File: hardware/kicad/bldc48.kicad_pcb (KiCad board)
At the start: 4 copper layers, 188 x 74 mm, 174 parts, among them J1 BAT+, J10 BRAKE, J11 POWER_BTN, J12 UART, J2 BAT-, J3 MOTOR_A, J4 MOTOR_B, J5 MOTOR_C, J6 SWD, J7 HALL, J8 THROTTLE, J9 FWD/REV, Q1 MMBTA92, Q2 MMBTA42, Q3 IPT015N10N5, Q4 IPT015N10N5, Q5 IPT015N10N5, Q6 IPT015N10N5, Q7 IPT015N10N5, Q8 IPT015N10N5, U1 LM5164DDA, U10 STM32G431CBT6, U2 LM5164DDA, U3 AP2112K-3.3, U4 LM5109BMA, U5 INA240A1D, U6 LM5109BMA, U7 INA240A1D, U8 LM5109BMA, U9 INA240A1D

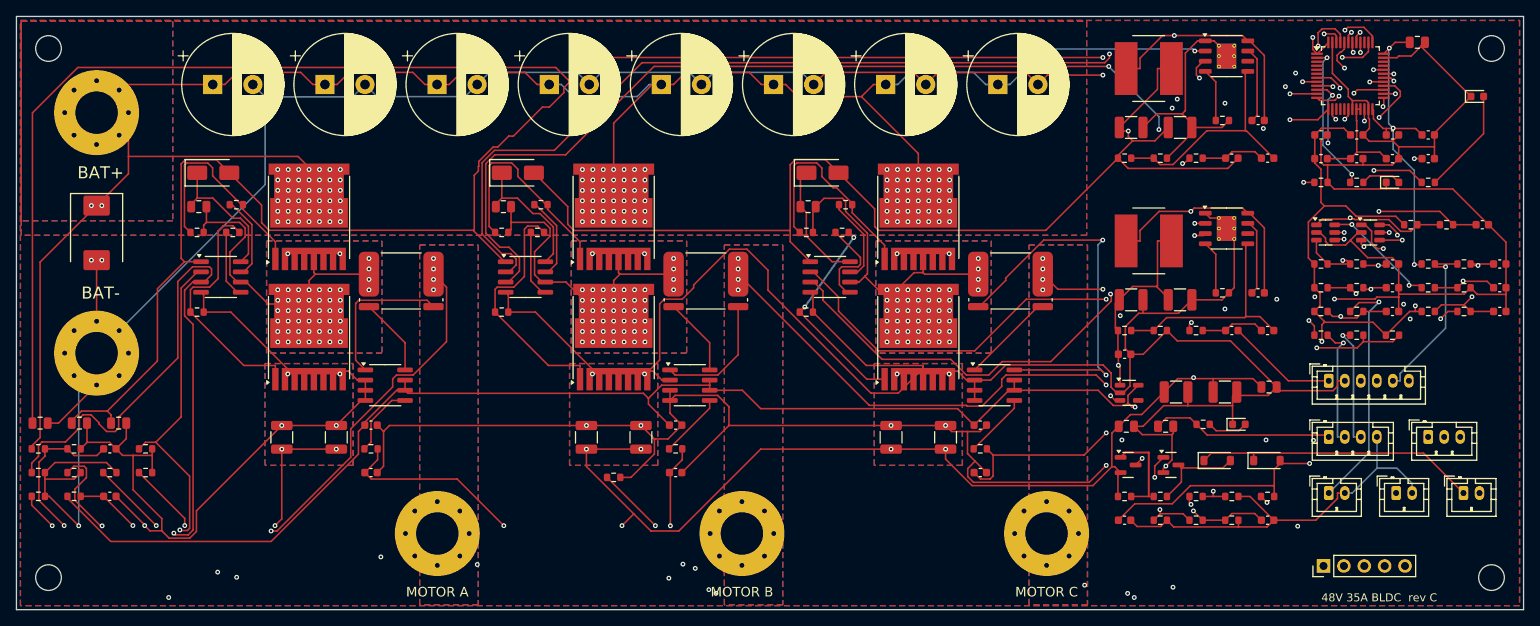
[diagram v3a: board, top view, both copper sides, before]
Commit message: Rev D: 185 x 66 mm board, routed, DRC clean, all parts stocked at LCSC
- Motor terminals beside the DC-link ceramics, routing channel underneath;
  17 mm battery strip; skyline-packed controller strip
- Phase strips free of signal tracks (both layers carry the motor current)
- Two INA240 supply taps the router left open closed with recorded routes
- Aishi ERS1KM221W25OT bulk caps (LCSC C106684)
- New renders, layer images, BOM, schematic PDF; README rev D + cost

Co-Authored-By: Claude Opus 5.5 <noreply@anthropic.com>
Claude-Session: https://claude.ai/code/session_01KE5bAkgcicsoh5erUtagKE
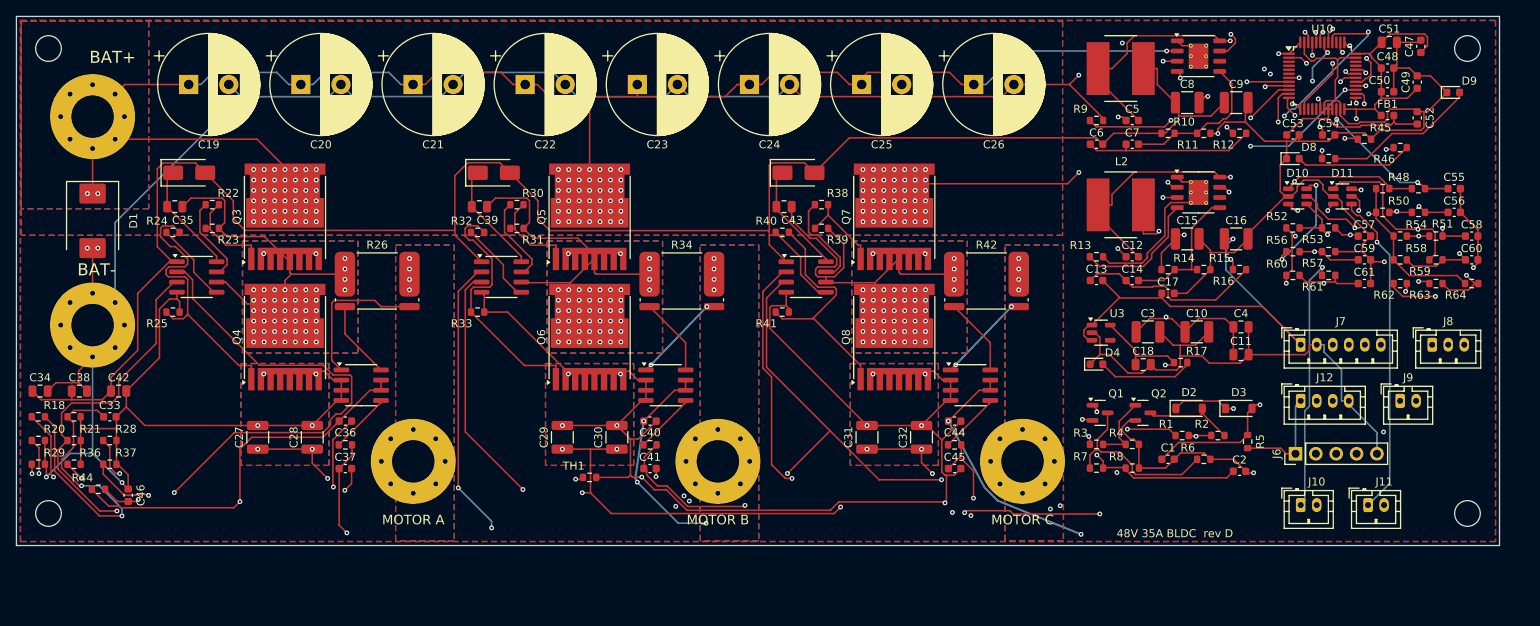
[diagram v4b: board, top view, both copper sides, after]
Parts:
- moved D4 19.3 mm to (134.7, 43.4)
- moved C13 18.0 mm to (134.7, 32.9)
- moved C14 18.0 mm to (139.2, 32.9)
- moved R52 17.5 mm to (159.2, 26.4)
- moved R56 17.5 mm to (159.2, 29.3)
- moved R60 17.5 mm to (159.2, 32.3)
- moved R53 17.5 mm to (163.7, 26.4)
- moved R57 17.5 mm to (163.7, 29.3)
- moved R61 17.5 mm to (163.7, 32.3)
- moved C57 17.2 mm to (168.1, 27.4)
- moved C59 17.2 mm to (168.1, 30.4)
- moved C61 17.2 mm to (168.1, 33.3)
- moved C6 17.0 mm to (134.7, 15.9)
- moved C7 17.0 mm to (139.2, 15.9)
- moved C11 16.9 mm to (152.7, 42.2)
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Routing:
- net +12V: track 440.4 -> 226.7 mm, vias 2 -> 0
- net PHASE_B: track 147.5 -> 0.00 mm, vias 5 -> 4
- net PWM_BH: track 357.1 -> 234.8 mm
- net GND: track 1050.7 -> 933.5 mm, vias 20 -> 27
- net PHASE_A: track 87.5 -> 0.00 mm, vias 5 -> 4
- net PWM_BL: track 336.3 -> 250.6 mm, vias 5 -> 4
- net PHASE_C: track 68.1 -> 0.00 mm, vias 5 -> 4
- net PWM_AL: track 292.4 -> 235.3 mm, vias 6 -> 4
- net ISP_C: track 48.4 -> 9.76 mm, vias 2 -> 0
- net PWM_AH: track 247.2 -> 284.2 mm, vias 5 -> 4
- net TEMP_FET: track 226.7 -> 194.6 mm, vias 5 -> 3
- net ISENSE_B: track 156.9 -> 127.0 mm
- net NRST: track 83.4 -> 58.0 mm
- net PWM_CL: track 279.2 -> 254.7 mm, vias 5 -> 6
- net HALL_C_IN: track 43.2 -> 23.4 mm, vias 2 -> 1
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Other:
- board size 188 x 74 mm -> 185 x 66 mm
- board text added: "48V 35A BLDC rev D"
- board text removed: "48V 35A BLDC rev C"

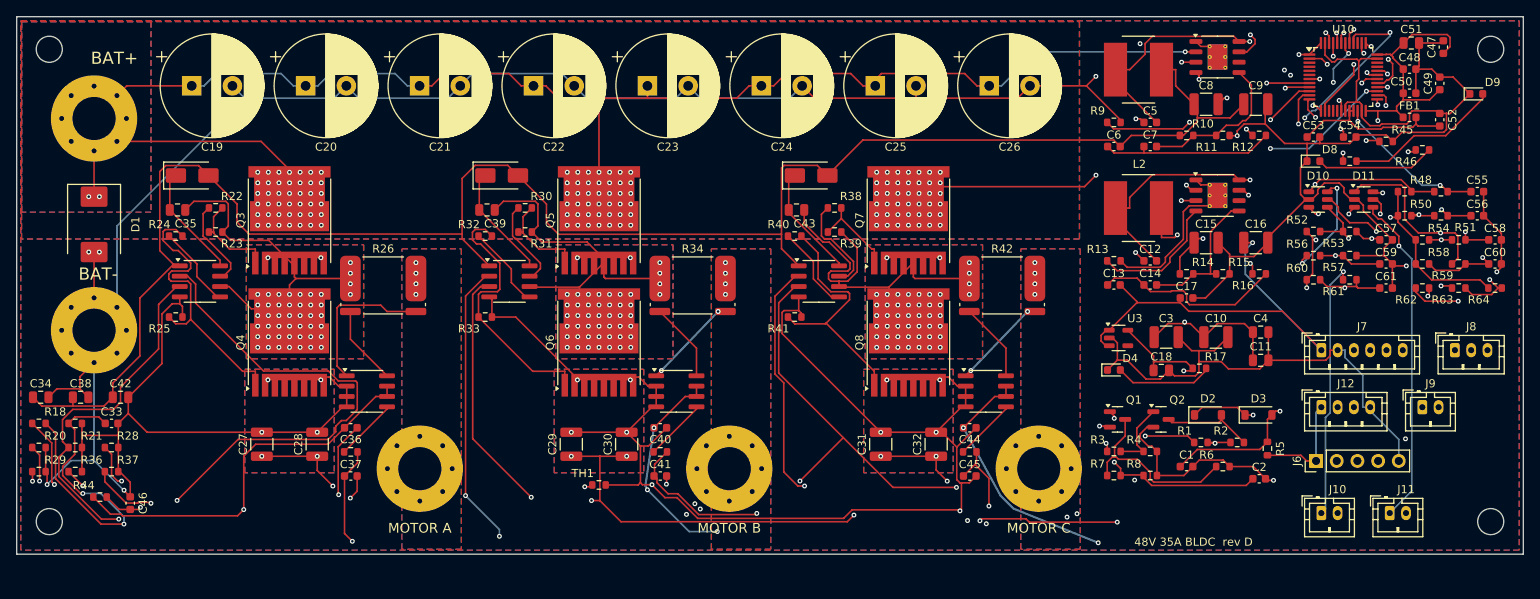
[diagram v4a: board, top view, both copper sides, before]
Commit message: Rev E: four 1000 uF/100 V bulk caps, 180 x 69.5 mm, routed, DRC clean
- 4 x Aishi ERS1KM102M35OT (LCSC C724666, 18 x 35 mm) spread over the
  bridges instead of 8 x 220 uF: 4000 uF, half the parts
- Rerouted (100 passes); the one open INA240 supply tap closed with a route
  from the new astar_route.py grid router, ending on a via into the +3V3 plane
- RIP_UP drops a 139 mm Freerouting detour on the phase C low-side gate drive;
  it is re-made locally (24 mm, like phases A/B). All phase and switch-node
  pours verified as one piece on both outer layers
- Stand-in 3D model for the 18 mm cans; new renders, layers, BOM, PDF, README

Co-Authored-By: Claude Opus 5.5 <noreply@anthropic.com>
Claude-Session: https://claude.ai/code/session_01KE5bAkgcicsoh5erUtagKE
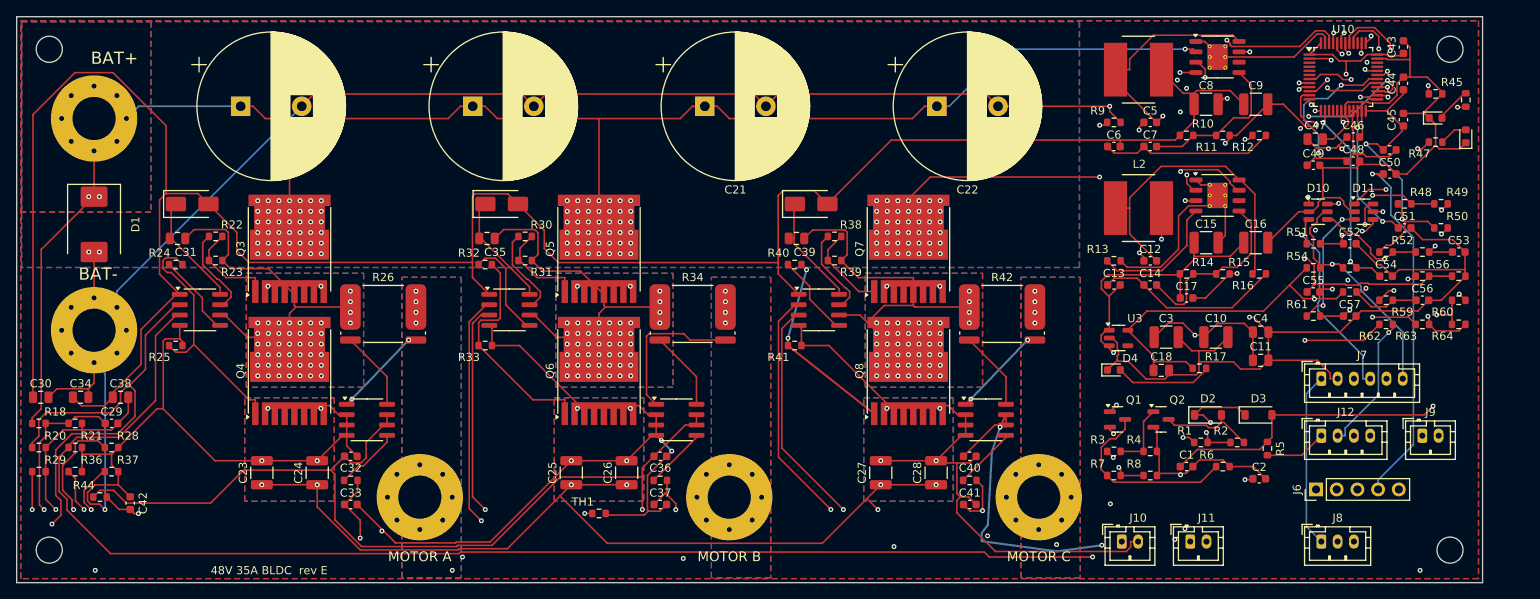
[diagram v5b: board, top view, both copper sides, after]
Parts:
- removed C58, C59, C60, C61: 100n, Capacitor_SMD:C_0603_1608Metric
- C19, C20, C21, C22: value 220u/100V -> 1000u/100V; footprint Capacitor_THT:CP_Radial_D12.5mm_P5.00mm -> Capacitor_THT:CP_Radial_D18.0mm_P7.50mm
- C23, C24, C25, C26: value 220u/100V -> 2.2u/100V; footprint Capacitor_THT:CP_Radial_D12.5mm_P5.00mm -> Capacitor_SMD:C_1210_3225Metric
- C29: value 2.2u/100V -> 10n; footprint Capacitor_SMD:C_1210_3225Metric -> Capacitor_SMD:C_0603_1608Metric
- C30: value 2.2u/100V -> 1u/25V; footprint Capacitor_SMD:C_1210_3225Metric -> Capacitor_SMD:C_0805_2012Metric
- C31: value 2.2u/100V -> 2.2u/25V; footprint Capacitor_SMD:C_1210_3225Metric -> Capacitor_SMD:C_0805_2012Metric
- C32: value 2.2u/100V -> 100n; footprint Capacitor_SMD:C_1210_3225Metric -> Capacitor_SMD:C_0603_1608Metric
- C33: value 10n -> 1n
- C42: value 1u/25V -> 100n; footprint Capacitor_SMD:C_0805_2012Metric -> Capacitor_SMD:C_0603_1608Metric
- C43: value 2.2u/25V -> 100n; footprint Capacitor_SMD:C_0805_2012Metric -> Capacitor_SMD:C_0603_1608Metric
- C45, C55, C56, C57: value 1n -> 100n
- C47: value 100n -> 4.7u; footprint Capacitor_SMD:C_0603_1608Metric -> Capacitor_SMD:C_0805_2012Metric
- C48: value 100n -> 1u
- C51: value 4.7u -> 1n; footprint Capacitor_SMD:C_0805_2012Metric -> Capacitor_SMD:C_0603_1608Metric
- C52: value 1u -> 1n
- C53: value 100n -> 1n
- moved C46 156.8 mm to (164.1, 14.8), turned to 0 degrees
- moved C31 90.0 mm to (19.7, 27.2), turned to 0 degrees
- moved C43 77.2 mm to (170.3, 3.73), turned to 90 degrees
- moved C27 76.1 mm to (106.1, 56.0)
- moved C28 76.1 mm to (112.9, 56.0)
- moved C24 72.3 mm to (36.9, 56.0), turned to 90 degrees
- moved C30 72.2 mm to (2.95, 46.7), turned to 0 degrees
- moved C32 71.9 mm to (41.0, 54.0), turned to 0 degrees
- moved C45 68.9 mm to (170.3, 12.6), turned to 90 degrees
- moved C44 68.0 mm to (170.3, 8.19), turned to 90 degrees
- moved C23 67.1 mm to (30.1, 56.0), turned to 90 degrees
- moved C26 65.1 mm to (74.9, 56.0), turned to 90 degrees
- moved C25 60.4 mm to (68.1, 56.0), turned to 90 degrees
- moved C29 56.5 mm to (11.6, 49.9), turned to 0 degrees
- moved C22 49.6 mm to (113.0, 11.0)
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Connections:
- C29 pad 1: +48V -> VBUS_SENSE
- C30 pad 1: +48V -> +12V
- C31 pad 1: +48V -> HB_A
- C31 pad 2: GND -> SW_A
- C32 pad 1: +48V -> +3V3
- C33 pad 1: VBUS_SENSE -> ISENSE_A
- C35 pad 1: HB_A -> HB_B
- C35 pad 2: SW_A -> SW_B
- C37 pad 1: ISENSE_A -> ISENSE_B
- C39 pad 1: HB_B -> HB_C
- C39 pad 2: SW_B -> SW_C
- C41 pad 1: ISENSE_B -> ISENSE_C
- C42 pad 1: +12V -> TEMP_FET
- C43 pad 1: HB_C -> +3V3
- C43 pad 2: SW_C -> GND
- C45 pad 1: ISENSE_C -> +3V3
- C46 pad 1: TEMP_FET -> +3V3
- C48 pad 1: +3V3 -> +3V3A
- C49 pad 1: +3V3 -> +3V3A
- C50 pad 1: +3V3 -> NRST
- C51 pad 1: +3V3 -> HALL_A
- C52 pad 1: +3V3A -> HALL_B
- C53 pad 1: +3V3A -> HALL_C
- C54 pad 1: NRST -> TEMP_MOTOR
- C55 pad 1: HALL_A -> THROTTLE
- C56 pad 1: HALL_B -> DIR_SW
- C57 pad 1: HALL_C -> BRAKE
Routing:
- net +12V: track 226.7 -> 283.7 mm
- net +3V3: track 392.9 -> 425.2 mm, vias 12 -> 11
- net PWM_BL: track 250.6 -> 278.4 mm, vias 4 -> 6
- net BRAKE_IN: track 40.3 -> 63.2 mm
- net THR_IN: track 39.1 -> 61.5 mm, vias 2 -> 3
- net +48V: track 521.6 -> 499.9 mm, vias 145 -> 141
- net TEMP_MOTOR: track 43.5 -> 24.3 mm
- net ISENSE_C: track 86.8 -> 104.6 mm, vias 2 -> 3
- net PWM_BH: track 234.8 -> 252.3 mm, vias 6 -> 5
- net THROTTLE: track 28.4 -> 44.7 mm
- net LED_FAULT_A: track 19.3 -> 3.51 mm
- net GND: track 933.5 -> 948.5 mm, vias 27 -> 26
- net PWM_AH: track 284.2 -> 269.5 mm
- net PWR_BTN: track 74.9 -> 89.2 mm, vias 3 -> 2
- net BRAKE: track 41.5 -> 55.3 mm
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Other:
- board size 185 x 66 mm -> 180 x 69.5 mm
- board text added: "48V 35A BLDC rev E"
- board text removed: "48V 35A BLDC rev D"
